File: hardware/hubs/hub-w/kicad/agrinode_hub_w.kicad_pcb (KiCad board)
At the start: 2 copper layers, 114 x 96 mm, 101 parts, among them J1 DC 12V 5.5/2.1, J2 DC IN 7-24V, J3 SOLAR 6-24V, J4 USB 5V / PROG, J5 BAT NTC 10k, J6 PROG, J7 I2C, J8 LED STRIP WS2813, J9 RS-485, Q1 AO3401A, Q2 AO3401A, Q3 MMBT3904, Q4 MMBT3904, Q5 BSS138, Q6 MMBT3904, SW1 RESET, SW2 BOOT / PAIR, U1 LM2596S-5.0, U2 TP4056, U3 MIC29302WU, U4 ESP32-WROOM-32E-N8, U5 CH340C, U6 DS3231MZ, U7 MAX3485ESA

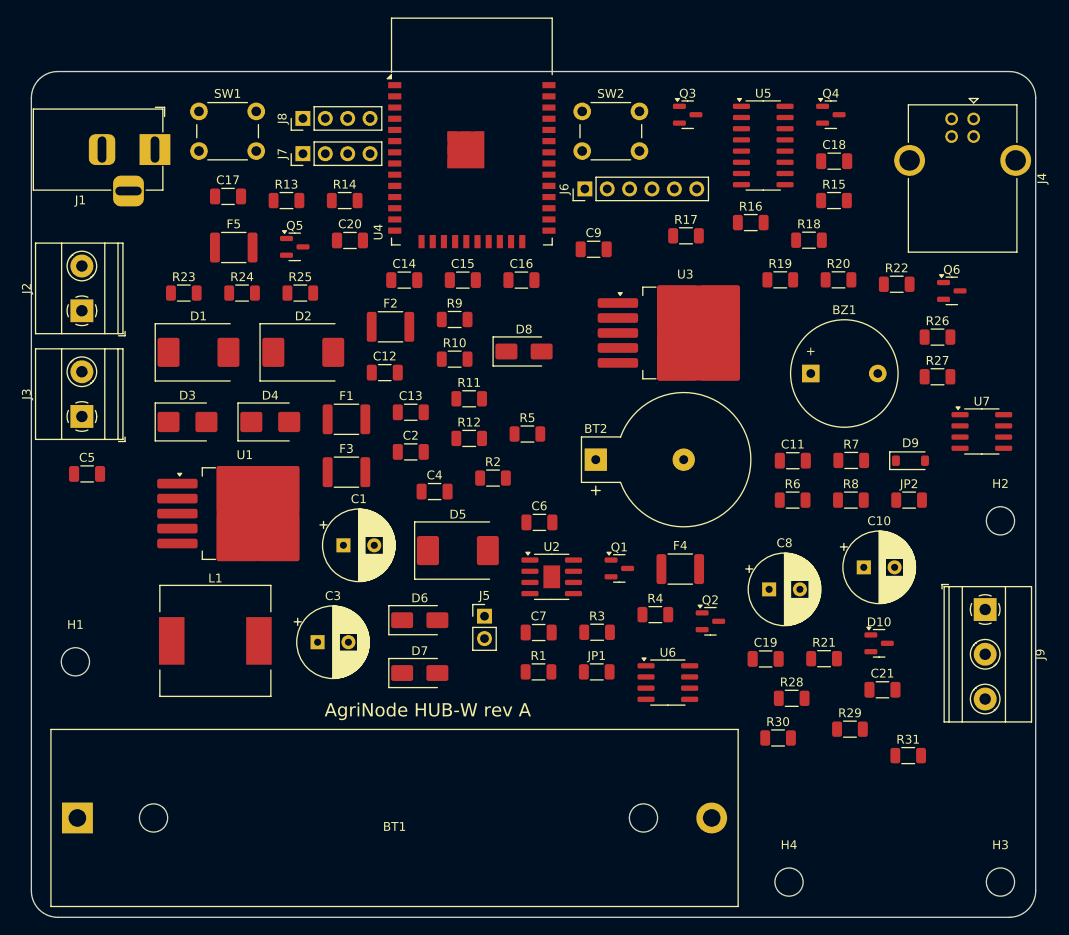
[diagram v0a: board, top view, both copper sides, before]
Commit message: hubs: intermediate routed boards (HUB-W 1 open connection; others in progress)
Co-Authored-By: Claude Opus 5.5 <noreply@anthropic.com>
Claude-Session: https://claude.ai/code/session_014J7amXZ5Y6AZWEh5CjDNja
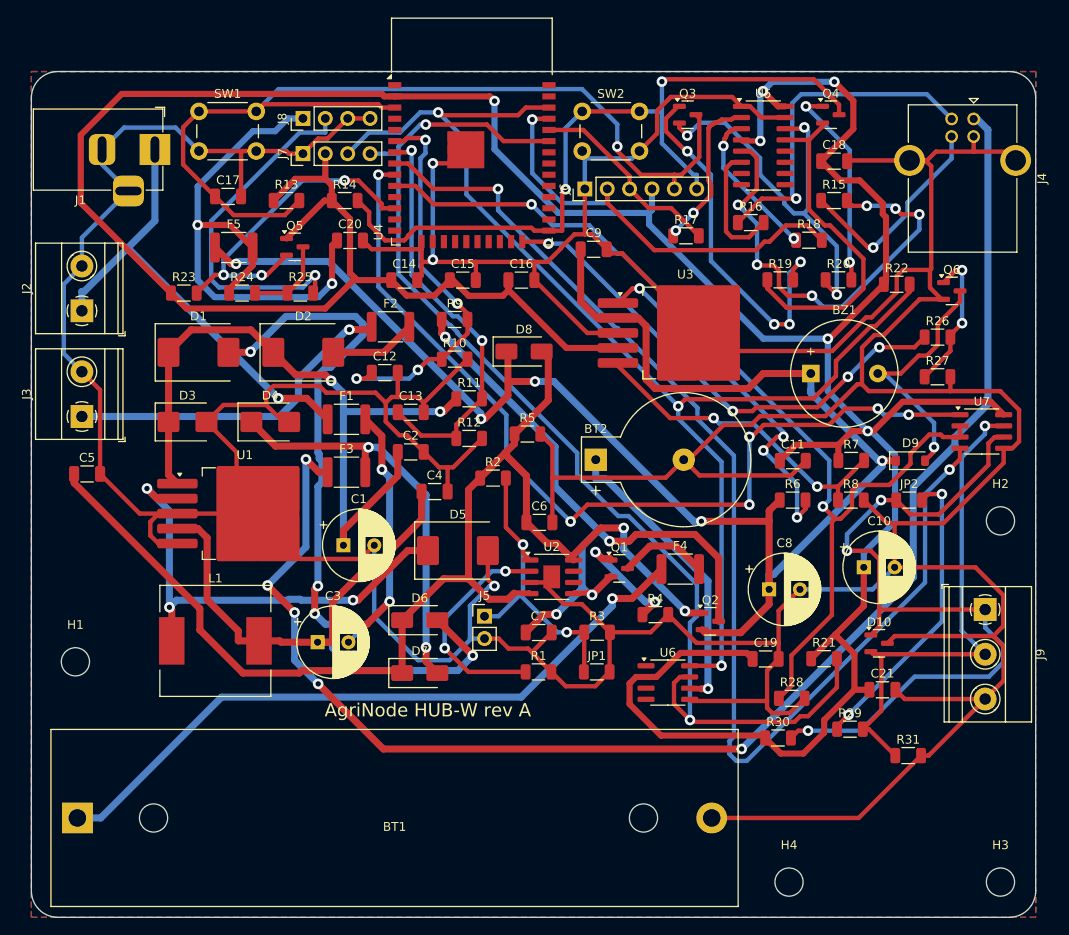
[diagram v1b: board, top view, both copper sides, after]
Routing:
- net GND: track 0.00 -> 778.0 mm, vias 0 -> 3
- net +3V3: track 0.00 -> 407.2 mm, vias 0 -> 6
- net VSYS: track 0.00 -> 181.4 mm, vias 0 -> 5
- net /Power - 12V, solar and USB inputs, 18650 charger, rails/VUSB_RAW: track 0.00 -> 167.9 mm, vias 0 -> 5
- net /Power - 12V, solar and USB inputs, 18650 charger, rails/V5: track 0.00 -> 140.1 mm, vias 0 -> 2
- net /ESP32, programming, buttons, RTC, LED strip, buzzer/I2C_SCL: track 0.00 -> 138.5 mm, vias 0 -> 3
- net RS485_TX: track 0.00 -> 136.3 mm, vias 0 -> 2
- net /ESP32, programming, buttons, RTC, LED strip, buzzer/I2C_SDA: track 0.00 -> 131.0 mm, vias 0 -> 2
- net RS485_DE: track 0.00 -> 114.0 mm, vias 0 -> 2
- net /ESP32, programming, buttons, RTC, LED strip, buzzer/ESP_EN: track 0.00 -> 110.3 mm, vias 0 -> 1
- net RS485_RX: track 0.00 -> 104.6 mm, vias 0 -> 6
- net /ESP32, programming, buttons, RTC, LED strip, buzzer/BOOT_BTN: track 0.00 -> 86.8 mm, vias 0 -> 2
- net /RS-485 and uplink/RS485_A: track 0.00 -> 86.6 mm, vias 0 -> 3
- net /Power - 12V, solar and USB inputs, 18650 charger, rails/VDC_F: track 0.00 -> 85.1 mm, vias 0 -> 6
- net /Power - 12V, solar and USB inputs, 18650 charger, rails/VIN_BUCK: track 0.00 -> 83.1 mm, vias 0 -> 2
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- added copper zone on B.Cu, net GND
- added copper zone on F.Cu, net GND

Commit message: hubs: boards after GPIO remap (placement; routing in progress)
Co-Authored-By: Claude Opus 5.5 <noreply@anthropic.com>
Claude-Session: https://claude.ai/code/session_014J7amXZ5Y6AZWEh5CjDNja
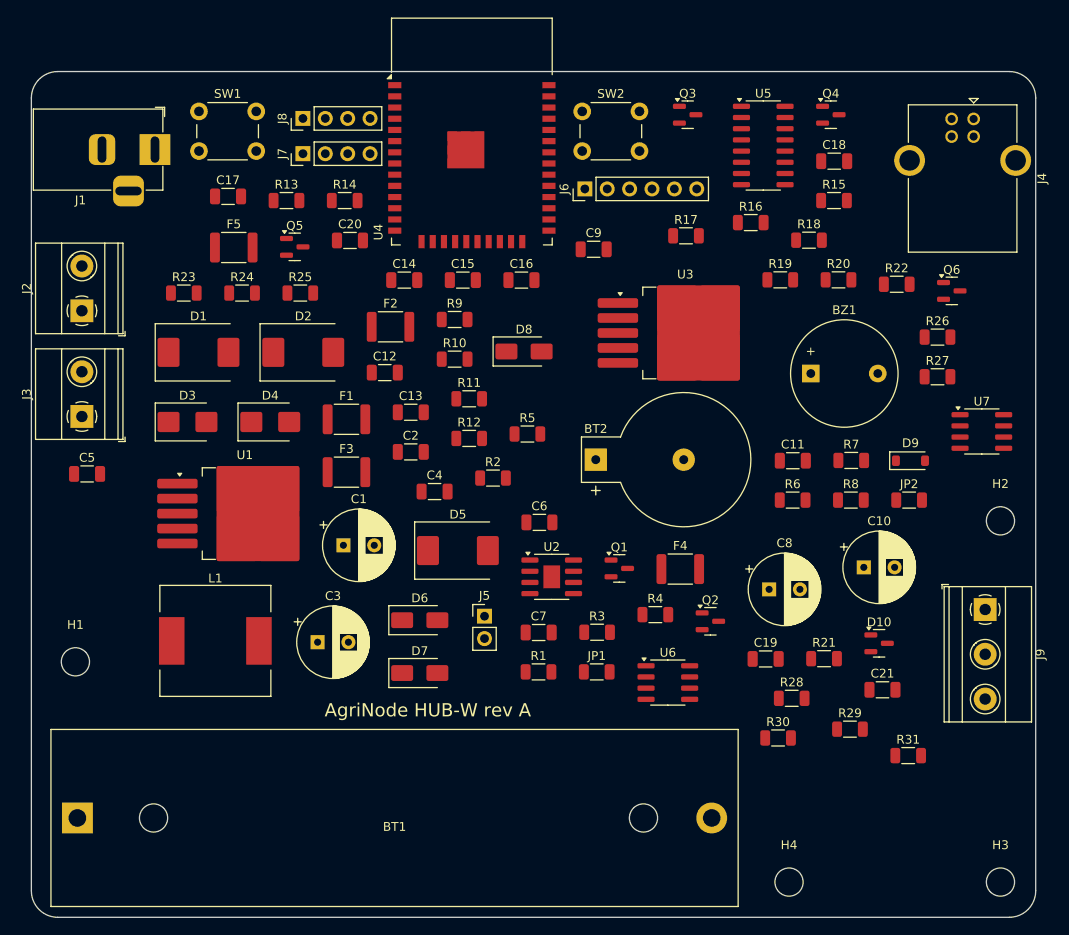
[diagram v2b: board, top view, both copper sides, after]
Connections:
- U4 pad 10: RS485_DE -> unconnected-(U4-IO25-Pad10)
- U4 pad 14: CHRG_N -> unconnected-(U4-IO12-Pad14)
- U4 pad 16: unconnected-(U4-IO13-Pad16) -> CHRG_N
- U4 pad 26: unconnected-(U4-IO4-Pad26) -> RS485_DE
- U4 pad 27: unconnected-(U4-IO16-Pad27) -> RS485_RX
- U4 pad 28: unconnected-(U4-IO17-Pad28) -> RS485_TX
- U4 pad 33: /ESP32, programming, buttons, RTC, LED strip, buzzer/I2C_SDA -> unconnected-(U4-IO21-Pad33)
- U4 pad 36: /ESP32, programming, buttons, RTC, LED strip, buzzer/I2C_SCL -> unconnected-(U4-IO22-Pad36)
- U4 pad 8: RS485_TX -> /ESP32, programming, buttons, RTC, LED strip, buzzer/I2C_SCL
- U4 pad 9: RS485_RX -> /ESP32, programming, buttons, RTC, LED strip, buzzer/I2C_SDA
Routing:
- net GND: track 778.0 -> 0.00 mm, vias 3 -> 0
- net +3V3: track 407.2 -> 0.00 mm, vias 6 -> 0
- net VSYS: track 181.4 -> 0.00 mm, vias 5 -> 0
- net /Power - 12V, solar and USB inputs, 18650 charger, rails/VUSB_RAW: track 167.9 -> 0.00 mm, vias 5 -> 0
- net /Power - 12V, solar and USB inputs, 18650 charger, rails/V5: track 140.1 -> 0.00 mm, vias 2 -> 0
- net /ESP32, programming, buttons, RTC, LED strip, buzzer/I2C_SCL: track 138.5 -> 0.00 mm, vias 3 -> 0
- net RS485_TX: track 136.3 -> 0.00 mm, vias 2 -> 0
- net /ESP32, programming, buttons, RTC, LED strip, buzzer/I2C_SDA: track 131.0 -> 0.00 mm, vias 2 -> 0
- net RS485_DE: track 114.0 -> 0.00 mm, vias 2 -> 0
- net /ESP32, programming, buttons, RTC, LED strip, buzzer/ESP_EN: track 110.3 -> 0.00 mm, vias 1 -> 0
- net RS485_RX: track 104.6 -> 0.00 mm, vias 6 -> 0
- net /ESP32, programming, buttons, RTC, LED strip, buzzer/BOOT_BTN: track 86.8 -> 0.00 mm, vias 2 -> 0
- net /RS-485 and uplink/RS485_A: track 86.6 -> 0.00 mm, vias 3 -> 0
- net /Power - 12V, solar and USB inputs, 18650 charger, rails/VDC_F: track 85.1 -> 0.00 mm, vias 6 -> 0
- net /Power - 12V, solar and USB inputs, 18650 charger, rails/VIN_BUCK: track 83.1 -> 0.00 mm, vias 2 -> 0
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- removed copper zone on B.Cu, net GND
- removed copper zone on F.Cu, net GND
